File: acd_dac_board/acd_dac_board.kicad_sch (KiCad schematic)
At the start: 4 parts, among them J1 Conn_02x10_Odd_Even, J2 Conn_02x10_Odd_Even, J3 Conn_02x10_Odd_Even, J4 Conn_02x25_Odd_Even

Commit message: update adc_dac board
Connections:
- net CLK is gone; now on net E13: J1.6 (Pin_6)
- net D0 is gone; now on net F14: J1.5 (Pin_5)
- net D1 is gone; now on net A12: J1.8 (Pin_8)
- net D2 is gone; now on net B12: J1.7 (Pin_7)
- net D3 is gone; now on net B11: J1.10 (Pin_10)
- net D4 is gone; now on net C11: J1.9 (Pin_9)
- net D5 is gone; now on net D10: J1.12 (Pin_12)
- net D6 is gone; now on net D11: J1.11 (Pin_11)
- net D7 is gone; now on net D9: J1.14 (Pin_14)
- net D8 is gone; now on net C9: J1.13 (Pin_13)
- net OTR is gone; now on net A9: J1.17 (Pin_17)
- net A10: now also J1.15 (Pin_15)
- net A15: now also J2.18 (Pin_18); no longer J2.14 (Pin_14)
- net A17: now also J2.14 (Pin_14); no longer J2.18 (Pin_18)
- net B10: now also J1.16 (Pin_16)
- net B15: now also J2.17 (Pin_17); no longer J2.13 (Pin_13)
- net B17: now also J2.13 (Pin_13); no longer J2.17 (Pin_17)
- net B9: now also J1.18 (Pin_18)
- net D10: no longer J1.15 (Pin_15)
- net D11: no longer J1.18 (Pin_18)
- net D9: no longer J1.16 (Pin_16)

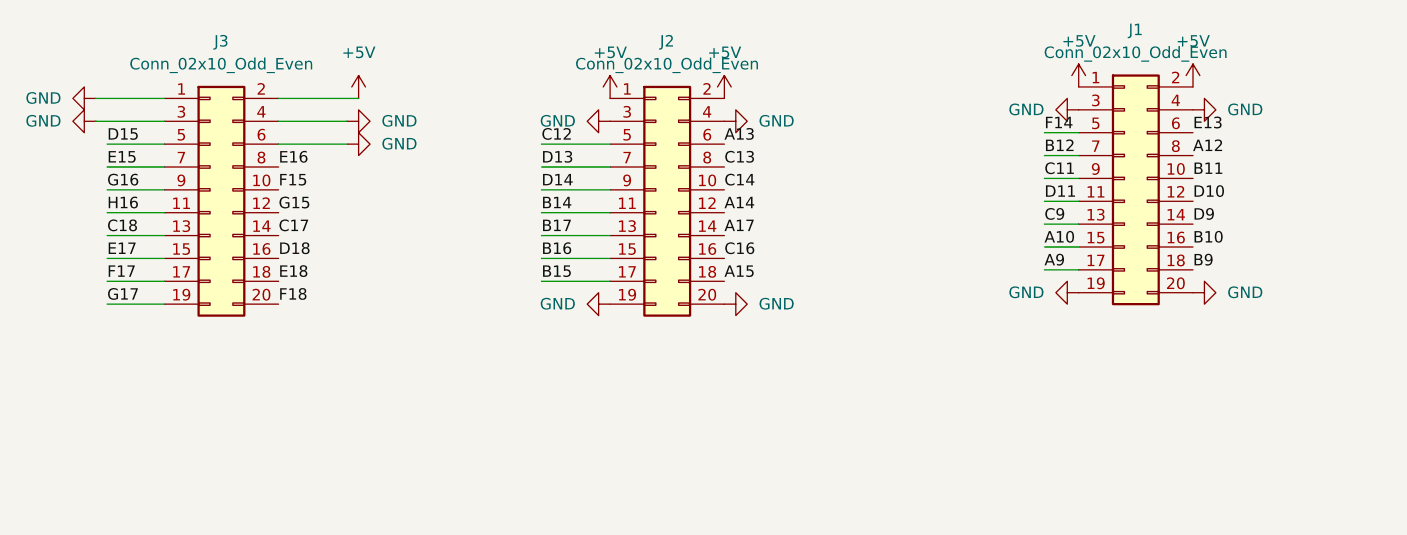
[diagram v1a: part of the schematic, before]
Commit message: route adc_dac board (fix errors). Finish first version of holder
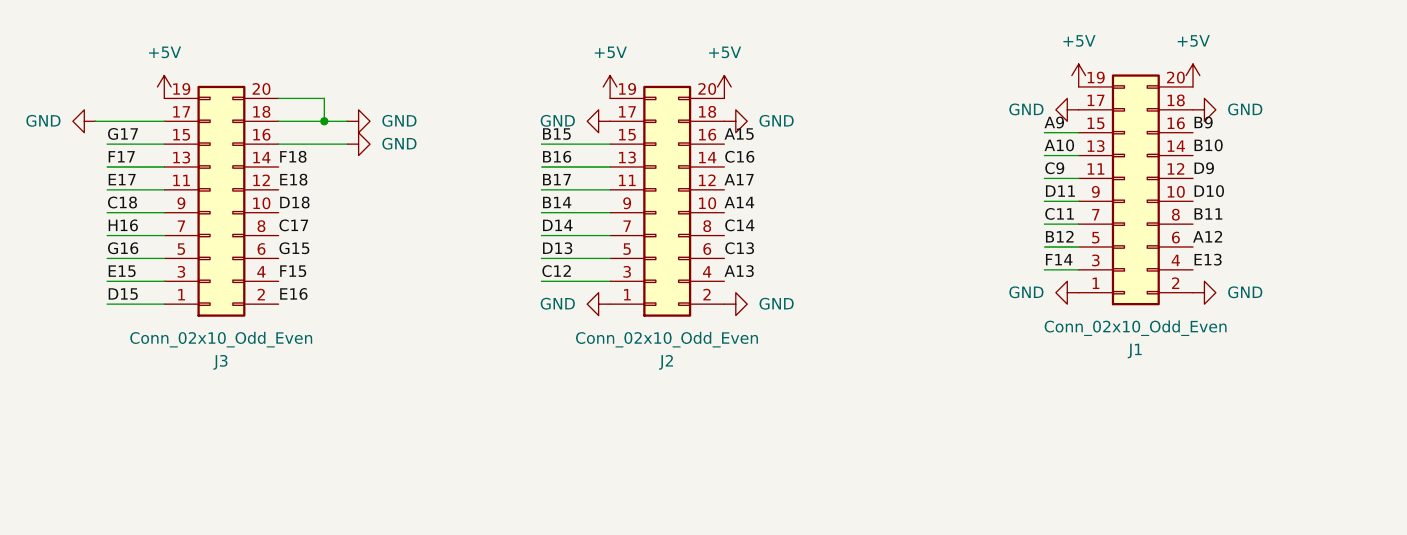
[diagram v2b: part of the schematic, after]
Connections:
- net +5V: now also J1.19 (Pin_19), J1.20 (Pin_20), J2.19 (Pin_19), J2.20 (Pin_20), J3.19 (Pin_19); no longer J1.1 (Pin_1), J1.2 (Pin_2), J2.1 (Pin_1), J2.2 (Pin_2), J3.2 (Pin_2)
- net A10: now also J1.13 (Pin_13); no longer J1.15 (Pin_15)
- net A12: now also J1.6 (Pin_6); no longer J1.8 (Pin_8)
- net A13: now also J2.4 (Pin_4); no longer J2.6 (Pin_6)
- net A14: now also J2.10 (Pin_10); no longer J2.12 (Pin_12)
- net A15: now also J2.16 (Pin_16); no longer J2.18 (Pin_18)
- net A17: now also J2.12 (Pin_12); no longer J2.14 (Pin_14)
- net A9: now also J1.15 (Pin_15); no longer J1.17 (Pin_17)
- net B10: now also J1.14 (Pin_14); no longer J1.16 (Pin_16)
- net B11: now also J1.8 (Pin_8); no longer J1.10 (Pin_10)
- net B12: now also J1.5 (Pin_5); no longer J1.7 (Pin_7)
- net B14: now also J2.9 (Pin_9); no longer J2.11 (Pin_11)
- net B15: now also J2.15 (Pin_15); no longer J2.17 (Pin_17)
- net B16: now also J2.13 (Pin_13); no longer J2.15 (Pin_15)
- net B17: now also J2.11 (Pin_11); no longer J2.13 (Pin_13)
- net B9: now also J1.16 (Pin_16); no longer J1.18 (Pin_18)
- net C11: now also J1.7 (Pin_7); no longer J1.9 (Pin_9)
- net C12: now also J2.3 (Pin_3); no longer J2.5 (Pin_5)
- net C13: now also J2.6 (Pin_6); no longer J2.8 (Pin_8)
- net C14: now also J2.8 (Pin_8); no longer J2.10 (Pin_10)
- net C16: now also J2.14 (Pin_14); no longer J2.16 (Pin_16)
- net C17: now also J3.8 (Pin_8); no longer J3.14 (Pin_14)
- net C18: now also J3.9 (Pin_9); no longer J3.13 (Pin_13)
- net C9: now also J1.11 (Pin_11); no longer J1.13 (Pin_13)
- net D10: now also J1.10 (Pin_10); no longer J1.12 (Pin_12)
- net D11: now also J1.9 (Pin_9); no longer J1.11 (Pin_11)
- net D13: now also J2.5 (Pin_5); no longer J2.7 (Pin_7)
- net D14: now also J2.7 (Pin_7); no longer J2.9 (Pin_9)
- net D15: now also J3.1 (Pin_1); no longer J3.5 (Pin_5)
- net D18: now also J3.10 (Pin_10); no longer J3.16 (Pin_16)
- net D9: now also J1.12 (Pin_12); no longer J1.14 (Pin_14)
- net E13: now also J1.4 (Pin_4); no longer J1.6 (Pin_6)
- net E15: now also J3.3 (Pin_3); no longer J3.7 (Pin_7)
- net E16: now also J3.2 (Pin_2); no longer J3.8 (Pin_8)
- net E17: now also J3.11 (Pin_11); no longer J3.15 (Pin_15)
- net E18: now also J3.12 (Pin_12); no longer J3.18 (Pin_18)
- net F14: now also J1.3 (Pin_3); no longer J1.5 (Pin_5)
- net F15: now also J3.4 (Pin_4); no longer J3.10 (Pin_10)
- net F17: now also J3.13 (Pin_13); no longer J3.17 (Pin_17)
- net F18: now also J3.14 (Pin_14); no longer J3.20 (Pin_20)
- net G15: now also J3.6 (Pin_6); no longer J3.12 (Pin_12)
- net G16: now also J3.5 (Pin_5); no longer J3.9 (Pin_9)
- net G17: now also J3.15 (Pin_15); no longer J3.19 (Pin_19)
- net GND: now also J1.1 (Pin_1), J1.17 (Pin_17), J1.18 (Pin_18), J1.2 (Pin_2), J2.1 (Pin_1), J2.17 (Pin_17), J2.18 (Pin_18), J2.2 (Pin_2), J3.16 (Pin_16), J3.17 (Pin_17), J3.18 (Pin_18), J3.20 (Pin_20); no longer J1.19 (Pin_19), J1.20 (Pin_20), J1.3 (Pin_3), J1.4 (Pin_4), J2.19 (Pin_19), J2.20 (Pin_20), J2.3 (Pin_3), J2.4 (Pin_4), J3.1 (Pin_1), J3.3 (Pin_3), J3.4 (Pin_4), J3.6 (Pin_6)
- net H16: now also J3.7 (Pin_7); no longer J3.11 (Pin_11)

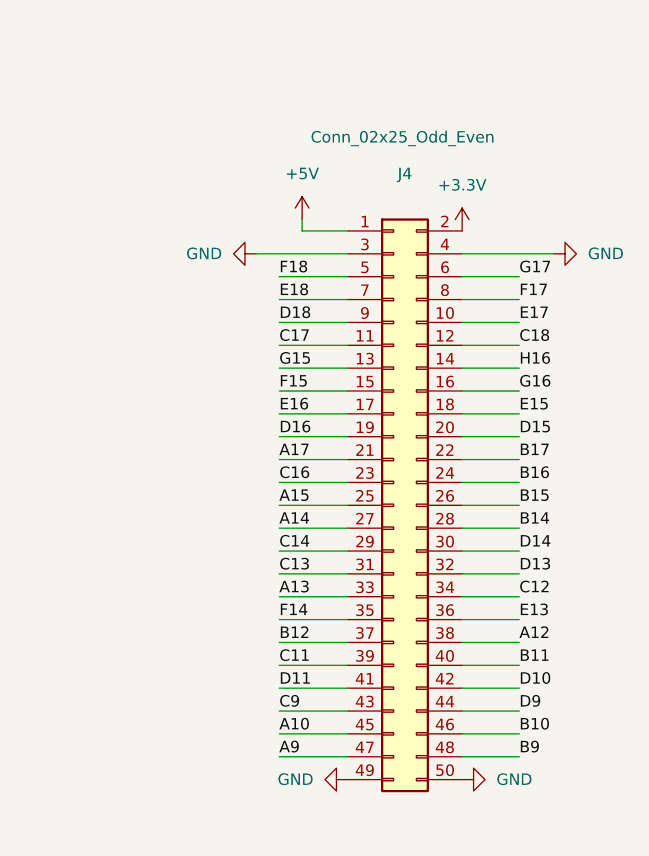
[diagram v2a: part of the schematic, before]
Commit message: fix adc board pinout
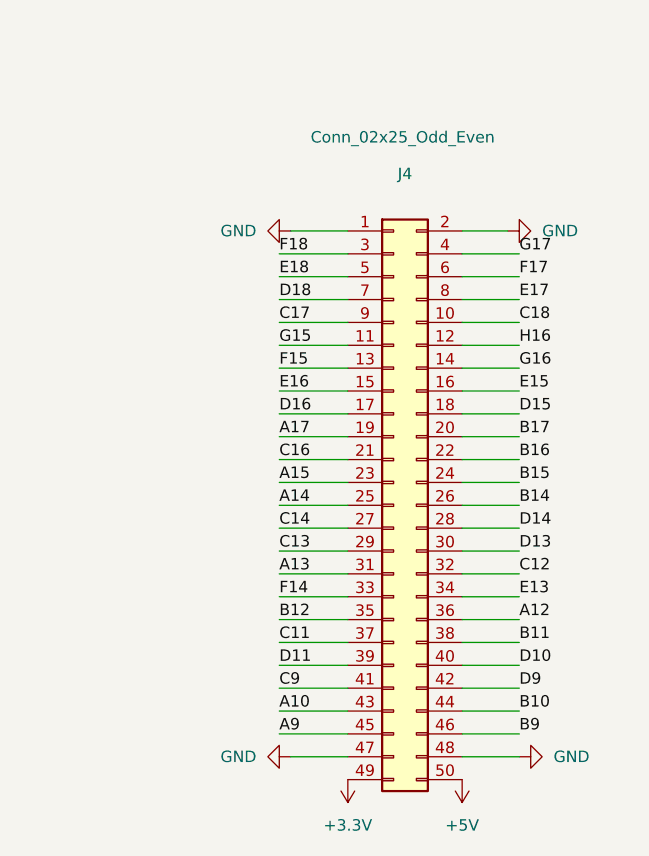
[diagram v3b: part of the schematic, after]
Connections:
- net +3.3V: now also J4.49 (Pin_49); no longer J4.2 (Pin_2)
- net +5V: now also J4.50 (Pin_50); no longer J4.1 (Pin_1)
- net A10: now also J4.43 (Pin_43); no longer J4.45 (Pin_45)
- net A12: now also J4.36 (Pin_36); no longer J4.38 (Pin_38)
- net A13: now also J4.31 (Pin_31); no longer J4.33 (Pin_33)
- net A14: now also J4.25 (Pin_25); no longer J4.27 (Pin_27)
- net A15: now also J4.23 (Pin_23); no longer J4.25 (Pin_25)
- net A17: now also J4.19 (Pin_19); no longer J4.21 (Pin_21)
- net A9: now also J4.45 (Pin_45); no longer J4.47 (Pin_47)
- net B10: now also J4.44 (Pin_44); no longer J4.46 (Pin_46)
- net B11: now also J4.38 (Pin_38); no longer J4.40 (Pin_40)
- net B12: now also J4.35 (Pin_35); no longer J4.37 (Pin_37)
- net B14: now also J4.26 (Pin_26); no longer J4.28 (Pin_28)
- net B15: now also J4.24 (Pin_24); no longer J4.26 (Pin_26)
- net B16: now also J4.22 (Pin_22); no longer J4.24 (Pin_24)
- net B17: now also J4.20 (Pin_20); no longer J4.22 (Pin_22)
- net B9: now also J4.46 (Pin_46); no longer J4.48 (Pin_48)
- net C11: now also J4.37 (Pin_37); no longer J4.39 (Pin_39)
- net C12: now also J4.32 (Pin_32); no longer J4.34 (Pin_34)
- net C13: now also J4.29 (Pin_29); no longer J4.31 (Pin_31)
- net C14: now also J4.27 (Pin_27); no longer J4.29 (Pin_29)
- net C16: now also J4.21 (Pin_21); no longer J4.23 (Pin_23)
- net C17: now also J4.9 (Pin_9); no longer J4.11 (Pin_11)
- net C18: now also J4.10 (Pin_10); no longer J4.12 (Pin_12)
- net C9: now also J4.41 (Pin_41); no longer J4.43 (Pin_43)
- net D10: now also J4.40 (Pin_40); no longer J4.42 (Pin_42)
- net D11: now also J4.39 (Pin_39); no longer J4.41 (Pin_41)
- net D13: now also J4.30 (Pin_30); no longer J4.32 (Pin_32)
- net D14: now also J4.28 (Pin_28); no longer J4.30 (Pin_30)
- net D15: now also J4.18 (Pin_18); no longer J4.20 (Pin_20)
- net D16: now also J4.17 (Pin_17); no longer J4.19 (Pin_19)
- net D18: now also J4.7 (Pin_7); no longer J4.9 (Pin_9)
- net D9: now also J4.42 (Pin_42); no longer J4.44 (Pin_44)
- net E13: now also J4.34 (Pin_34); no longer J4.36 (Pin_36)
- net E15: now also J4.16 (Pin_16); no longer J4.18 (Pin_18)
- net E16: now also J4.15 (Pin_15); no longer J4.17 (Pin_17)
- net E17: now also J4.8 (Pin_8); no longer J4.10 (Pin_10)
- net E18: now also J4.5 (Pin_5); no longer J4.7 (Pin_7)
- net F14: now also J4.33 (Pin_33); no longer J4.35 (Pin_35)
- net F15: now also J4.13 (Pin_13); no longer J4.15 (Pin_15)
- net F17: now also J4.6 (Pin_6); no longer J4.8 (Pin_8)
- net F18: now also J4.3 (Pin_3); no longer J4.5 (Pin_5)
- net G15: now also J4.11 (Pin_11); no longer J4.13 (Pin_13)
- net G16: now also J4.14 (Pin_14); no longer J4.16 (Pin_16)
- net G17: now also J4.4 (Pin_4); no longer J4.6 (Pin_6)
- net GND: now also J4.1 (Pin_1), J4.2 (Pin_2), J4.47 (Pin_47), J4.48 (Pin_48); no longer J4.3 (Pin_3), J4.4 (Pin_4), J4.49 (Pin_49), J4.50 (Pin_50)
- net H16: now also J4.12 (Pin_12); no longer J4.14 (Pin_14)
